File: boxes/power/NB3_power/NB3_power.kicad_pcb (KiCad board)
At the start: 2 copper layers, 50 x 44 mm, 31 parts, among them J1 Barrel_Jack_PJ-036AH-SMT-TR, J2 Conn_01x04_Male, SW1 SW_SPDT, U1 Voltage_Regulator_AP64501

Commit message: Final draft (rev 0.0.1) of NB3_power PCB
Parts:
- added D2: LED, LED_SMD:LED_0603_1608Metric, F.Cu at (132.0, 95.0)
- added G***: LOGO, NB3_power:Logo_VK_15mm, B.Cu at (155.0, 120.0)
- added R6: 1.6k, Resistor_SMD:R_0402_1005Metric, F.Cu at (131.2, 93.0)
- J2: footprint Connector_PinHeader_2.54mm:PinHeader_1x04_P2.54mm_Vertical_SMD_Pin1Right -> NB3_power:PinHeader_TSM-104-01-L-SH
- moved J2 24.3 mm to (178.1, 108.0), turned to -90 degrees
- moved H3 22.7 mm to (133.5, 127.0)
- moved D1 22.7 mm to (132.0, 97.0)
- moved H1 22.7 mm to (133.5, 89.0)
- moved J1 22.7 mm to (146.0, 107.7)
- moved SW1 22.7 mm to (135.0, 120.0)
- moved H4 22.7 mm to (176.5, 127.0)
- moved H2 22.7 mm to (176.5, 89.0)
- moved R1 22.7 mm to (131.2, 98.9)
- moved C1 21.8 mm to (152.5, 109.3)
- moved C10 21.8 mm to (168.2, 107.3)
- moved C11 21.8 mm to (166.5, 110.6)
- moved C12 21.8 mm to (162.5, 100.7)
- moved C13 21.8 mm to (160.0, 100.7)
- moved C14 21.8 mm to (160.0, 96.7)
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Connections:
- J2 pad 1: GND -> +5V
- J2 pad 2: GND -> +5V
- J2 pad 3: +5V -> GND
- J2 pad 4: +5V -> GND
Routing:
- net +5V: track 19.0 -> 45.5 mm, vias 0 -> 2
- net Net-(D2-Pad1): track 0.00 -> 1.50 mm
- net Net-(SW1-Pad2): track 37.0 -> 36.1 mm
- net GND: vias 14 -> 20
- added copper zone on B.Cu, net GND
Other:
- board text added: "+5V"
- board text added: "DC-DC Power Supply"
- board text added: "GND"
- board text added: "INPUT PWR"
- board text added: "Input: +6 to +36 Volt"
- board text added: "NB3_power Rev 0.0.1"
- board text added: "OFF - ON"
- board text added: "OUTPUT PWR"
- board text added: "Output: +5 Volt (5 Amp)"
- board text removed: "PWR"

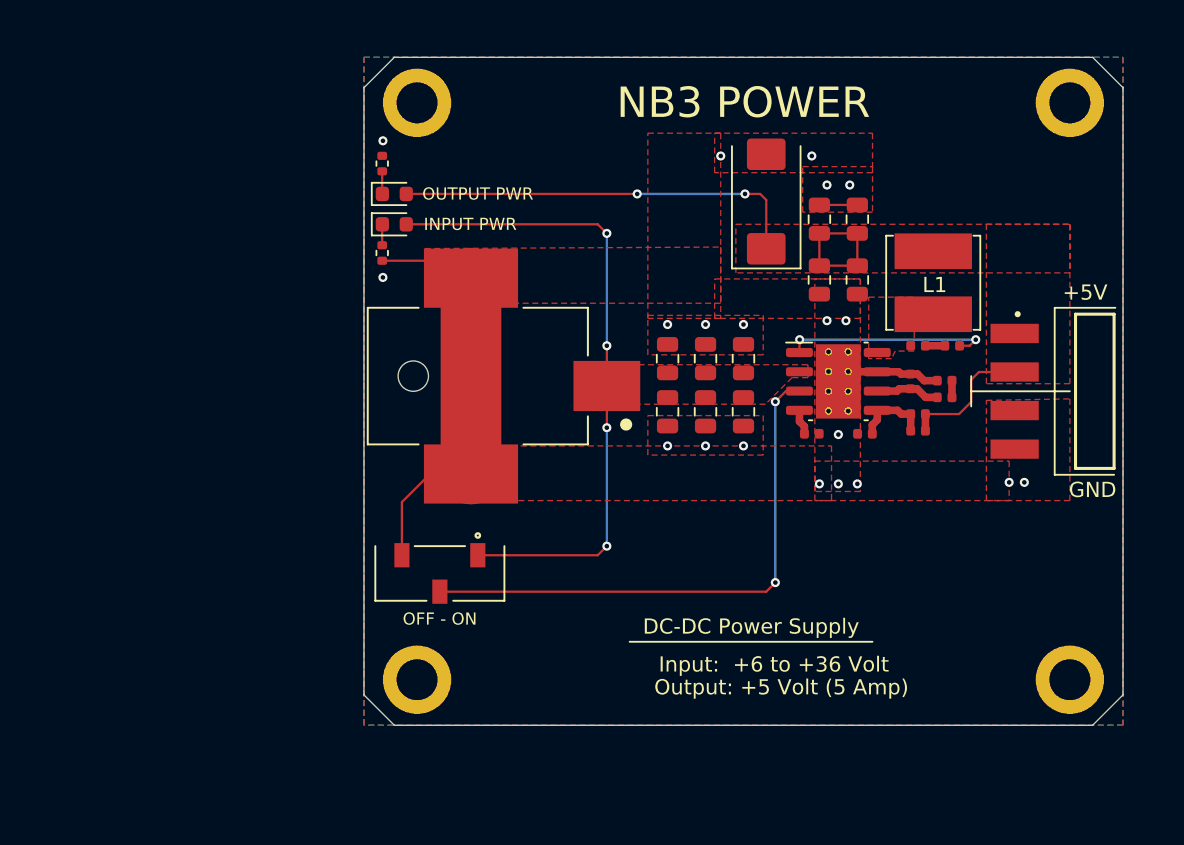
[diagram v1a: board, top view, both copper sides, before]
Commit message: Optimized NB3_power BOM for cost
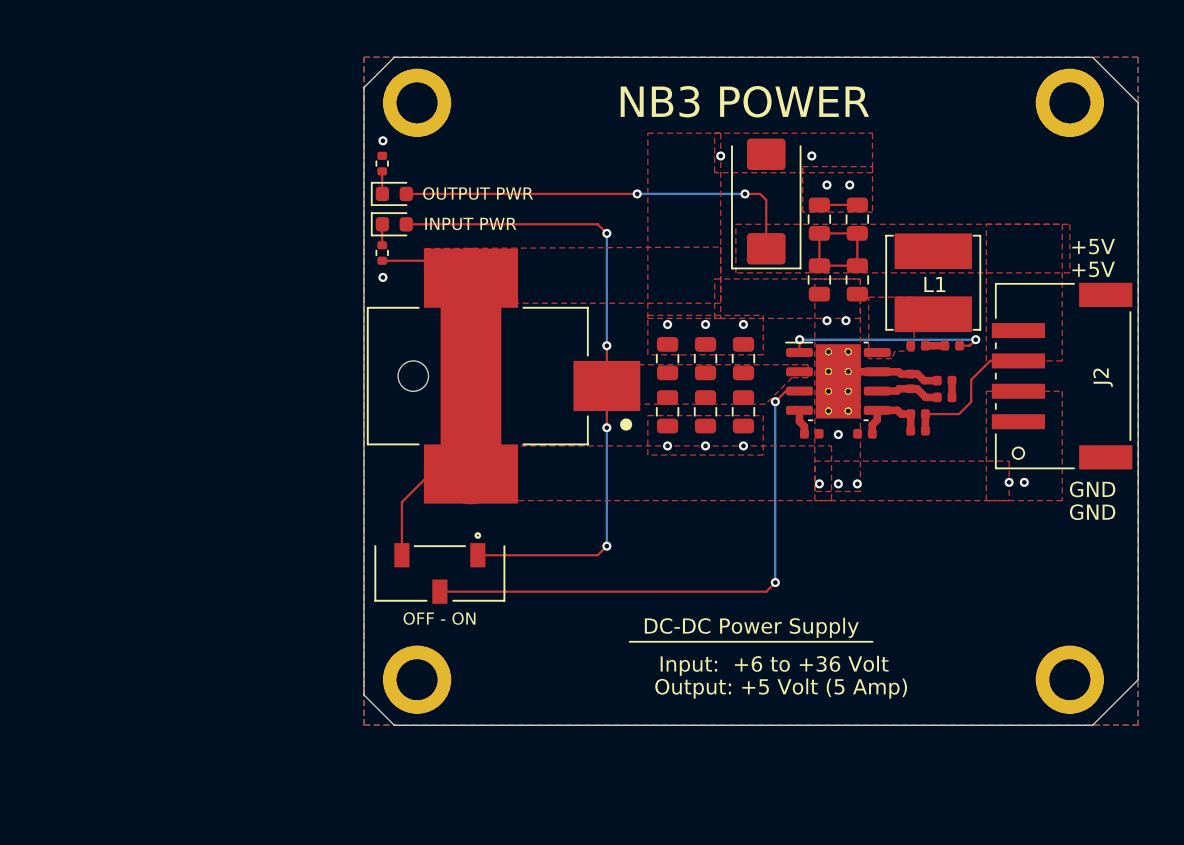
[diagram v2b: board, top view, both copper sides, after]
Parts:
- D1: value LED -> LED (Green)
- D2: value LED -> LED (Red)
- J2: value Conn_01x04_Male -> Connector_S4B-PH-SM4-TB(LF)(SN); footprint NB3_power:PinHeader_TSM-104-01-L-SH -> NB3_power:Connector_S4B-PH-SM4-TB(LF)(SN)
- moved G*** 9.01 mm to (164.0, 119.5)
- moved J2 2.31 mm to (176.1, 107.0)
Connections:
- J2 pad 1: +5V -> GND
- J2 pad 2: +5V -> GND
- J2 pad 3: GND -> +5V
- J2 pad 4: GND -> +5V
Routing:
- net +5V: track 45.5 -> 46.4 mm
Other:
- board size 50 x 44 mm -> 51 x 44 mm

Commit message: NB3 pcb design tweaks
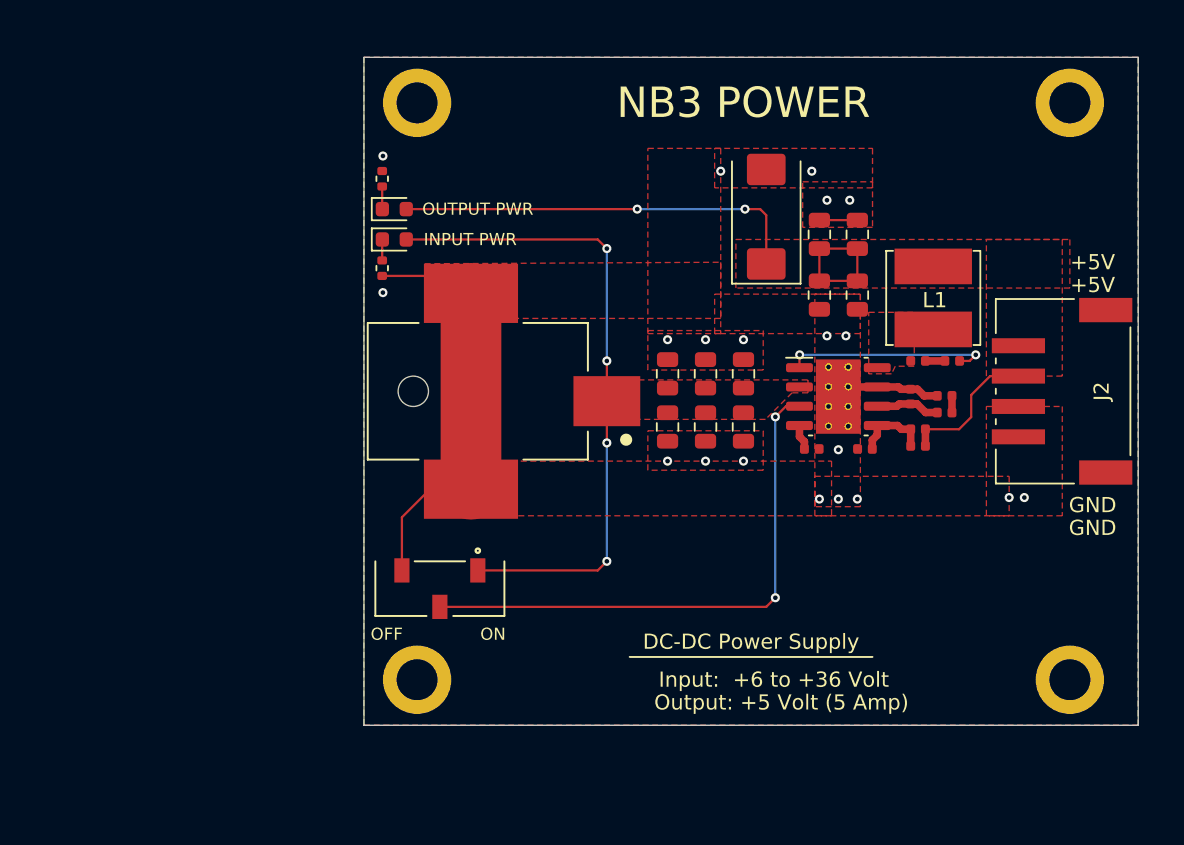
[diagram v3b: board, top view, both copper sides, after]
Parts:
- moved C1 1.00 mm to (152.5, 110.3)
- moved C10 1.00 mm to (168.2, 108.3)
- moved C11 1.00 mm to (166.5, 111.6)
- moved C12 1.00 mm to (162.5, 101.7)
- moved C13 1.00 mm to (160.0, 101.7)
- moved C14 1.00 mm to (160.0, 97.7)
- moved C15 1.00 mm to (162.5, 97.7)
- moved C16 1.00 mm to (156.5, 96.5)
- moved C2 1.00 mm to (155.0, 110.3)
- moved C3 1.00 mm to (150.0, 110.3)
- moved C4 1.00 mm to (150.0, 106.8)
- moved C5 1.00 mm to (152.5, 106.8)
- moved C6 1.00 mm to (155.0, 106.8)
- moved C7 1.00 mm to (168.8, 106.0)
- moved C8 1.00 mm to (159.5, 111.8)
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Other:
- outline, holes or cut-outs redrawn
- board text added: "NB3_power Rev 0.0.2"
- board text added: "OFF"
- board text added: "ON"
- board text removed: "NB3_power Rev 0.0.1"
- board text removed: "OFF - ON"

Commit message: Updated NB3_power: compatible w/replacement PS
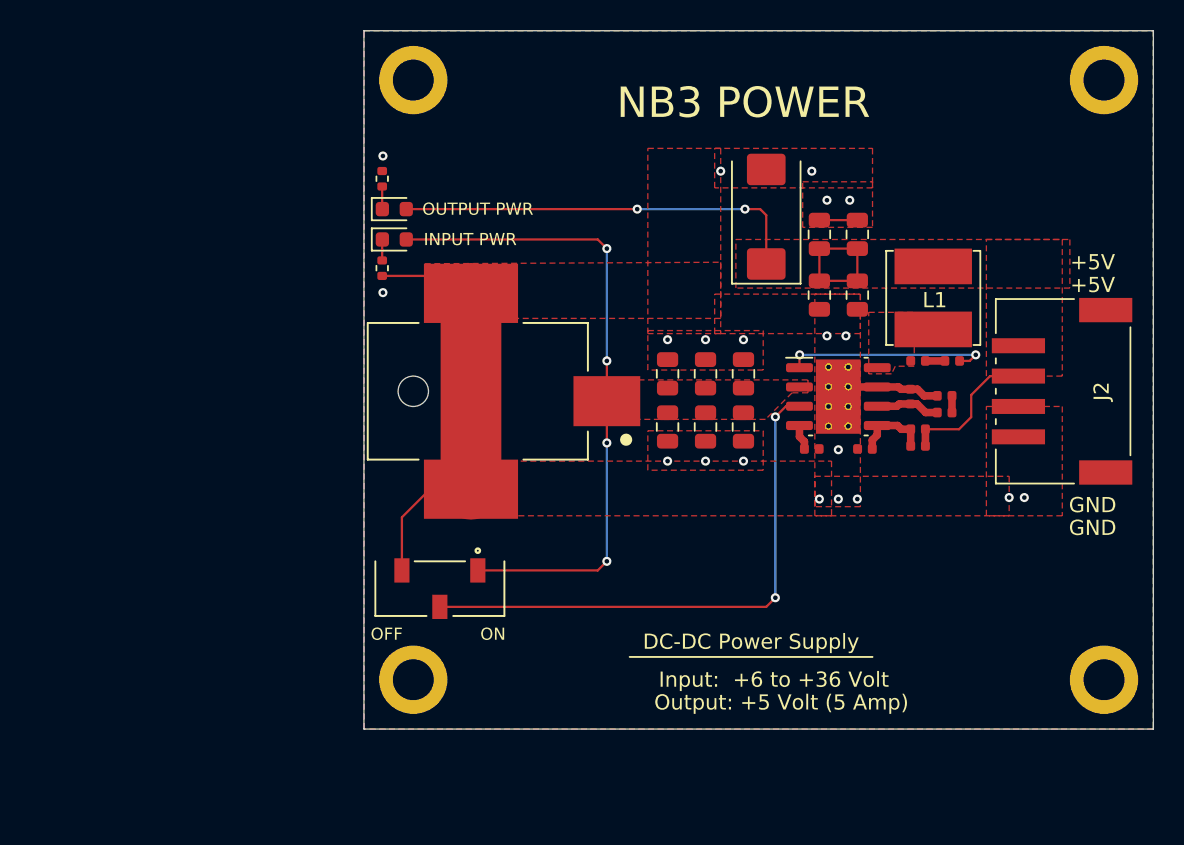
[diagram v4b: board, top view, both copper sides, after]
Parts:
- moved H2 2.70 mm to (178.8, 87.5)
- moved H4 2.25 mm to (178.8, 127.0)
- moved H1 1.52 mm to (133.2, 87.5)
- moved H3 0.25 mm to (133.2, 127.0)
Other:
- board size 51 x 44 mm -> 52 x 46 mm
- board text added: "NB3_power Rev 0.0.3"
- board text removed: "NB3_power Rev 0.0.2"

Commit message: Update NB3_body: new power dimensions
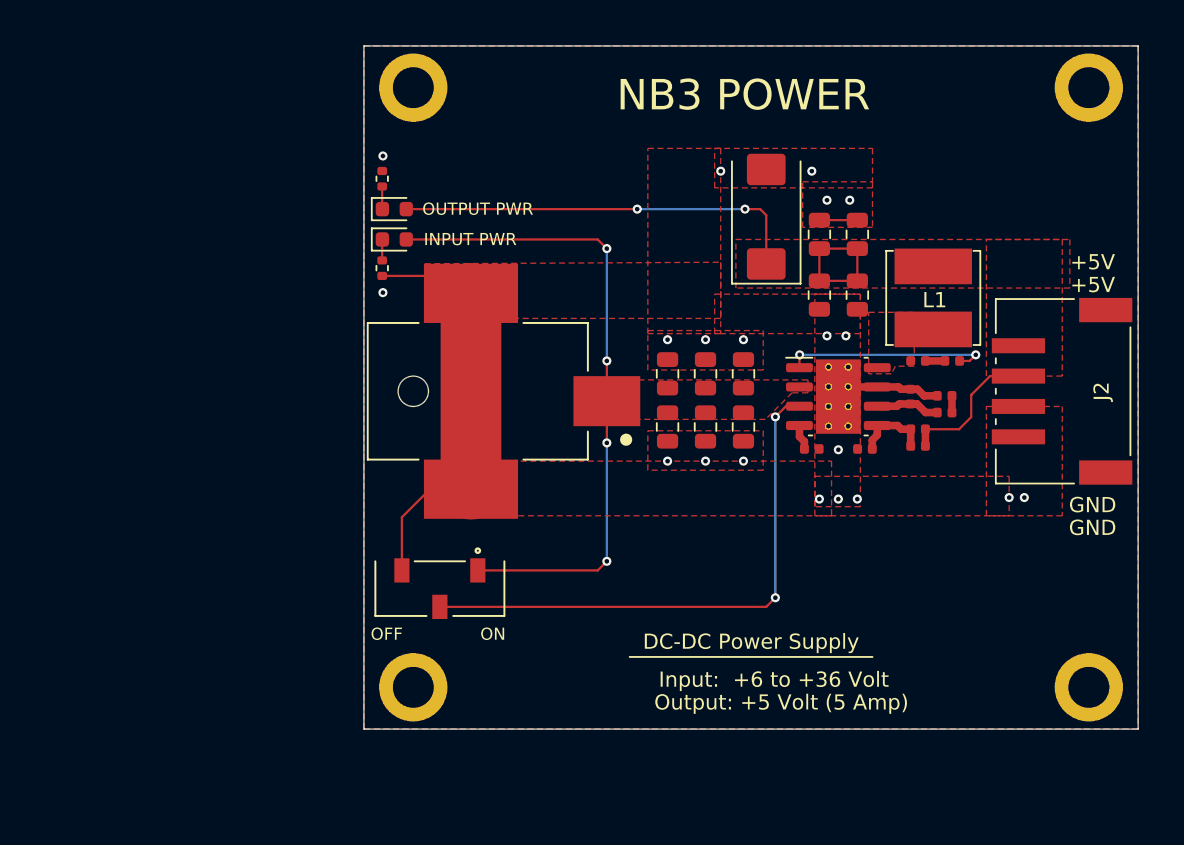
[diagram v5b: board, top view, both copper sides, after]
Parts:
- moved H2 1.12 mm to (177.8, 88.0)
- moved H4 1.12 mm to (177.8, 127.5)
- moved H1 0.50 mm to (133.2, 88.0)
- moved H3 0.50 mm to (133.2, 127.5)
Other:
- board size 52 x 46 mm -> 51 x 45 mm
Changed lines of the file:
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@@
   (net 13 "Net-(D2-Pad1)")
   (footprint "MountingHole:MountingHole_2.7mm_M2.5_ISO7380_Pad" (layer "F.Cu")
-    (at 133.25 127)
+    (at 133.25 127.5)
     (descr "Mounting Hole 2.7mm, M2.5, ISO7380")
     (tags "mounting hole 2.7mm m2.5 iso7380")
@@
   )
   (footprint "MountingHole:MountingHole_2.7mm_M2.5_ISO7380_Pad" (layer "F.Cu")
-    (at 178.75 87.5)
+    (at 177.75 88)
     (descr "Mounting Hole 2.7mm, M2.5, ISO7380")
     (tags "mounting hole 2.7mm m2.5 iso7380")
@@
   )
   (footprint "MountingHole:MountingHole_2.7mm_M2.5_ISO7380_Pad" (layer "F.Cu")
-    (at 178.75 127)
+    (at 177.75 127.5)
     (descr "Mounting Hole 2.7mm, M2.5, ISO7380")
     (tags "mounting hole 2.7mm m2.5 iso7380")
@@
   )
   (footprint "MountingHole:MountingHole_2.7mm_M2.5_ISO7380_Pad" (layer "F.Cu")
-    (at 133.25 87.5)
+    (at 133.25 88)
     (descr "Mounting Hole 2.7mm, M2.5, ISO7380")
     (tags "mounting hole 2.7mm m2.5 iso7380")
@@
   )
   (gr_line (start 147.5 125.5) (end 163.5 125.5) (layer "F.SilkS") (width 0.12))
-  (gr_rect (start 130 130.25) (end 182 84.25) (layer "Edge.Cuts") (width 0.05) (fill none))
+  (gr_rect (start 130 130.25) (end 181 85.25) (layer "Edge.Cuts") (width 0.05) (fill none))
   (gr_text "NB3_power\nRev 0.0.3" (at 141.5 127.5) (layer "B.SilkS")
     (effects (font (size 1 1) (thickness 0.15)) (justify mirror))
   )
-  (gr_text "NB3 POWER" (at 155 89) (layer "F.SilkS")
+  (gr_text "NB3 POWER" (at 155 88.5) (layer "F.SilkS")
     (effects (font (size 2 2) (thickness 0.3)))
   )
@@
     (effects (font (size 1 1) (thickness 0.15)))
   )
-  (target plus (at 130 130.25) (size 5) (width 0.05) (layer "Edge.Cuts"))
   (segment (start 162.5 96.725) (end 160 96.725) (width 0.15) (layer "F.Cu") (net 1))
   (segment (start 163.8125 107.715) (end 165.215 107.715) (width 0.5) (layer "F.Cu") (net 1))
@@
     (polygon
       (pts
-        (xy 182 130.25)
+        (xy 181 130.25)
         (xy 130 130.25)
-        (xy 130 84.25)
-        (xy 182 84.25)
+        (xy 130 85.25)
+        (xy 181 85.25)
       )
     )

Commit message: Update NB3_power (R&E Only)
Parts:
- moved G*** 25.0 mm to (167.5, 95.8)
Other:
- board text added: "For Research and Education ONLY"
- board text added: "NB3_power Rev 0.0.4"
- board text removed: "NB3_power Rev 0.0.3"
